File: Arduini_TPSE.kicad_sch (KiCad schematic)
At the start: 29 parts, among them J1 2134441-2, J2 ICSP, P1 Digital, P2 Analog, P3 CONN_01X01, P4 CONN_01X01, P5 CONN_01X01, P6 CONN_01X01, SW1 SW_Push, U1 AMS1117-3.3, U2 FT232RL, U3 ATmega328-P, U4 AMS1117-5.0, Y1 16Mhz

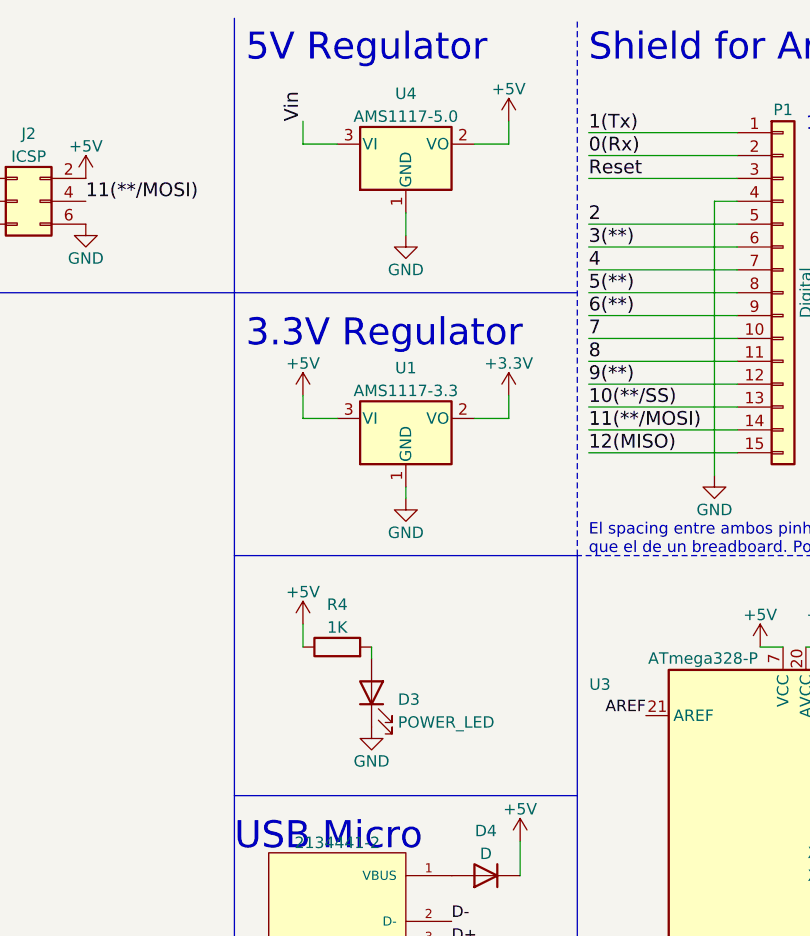
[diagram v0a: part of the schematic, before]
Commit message: Condensadores 3V3, 5V, y recolocacion
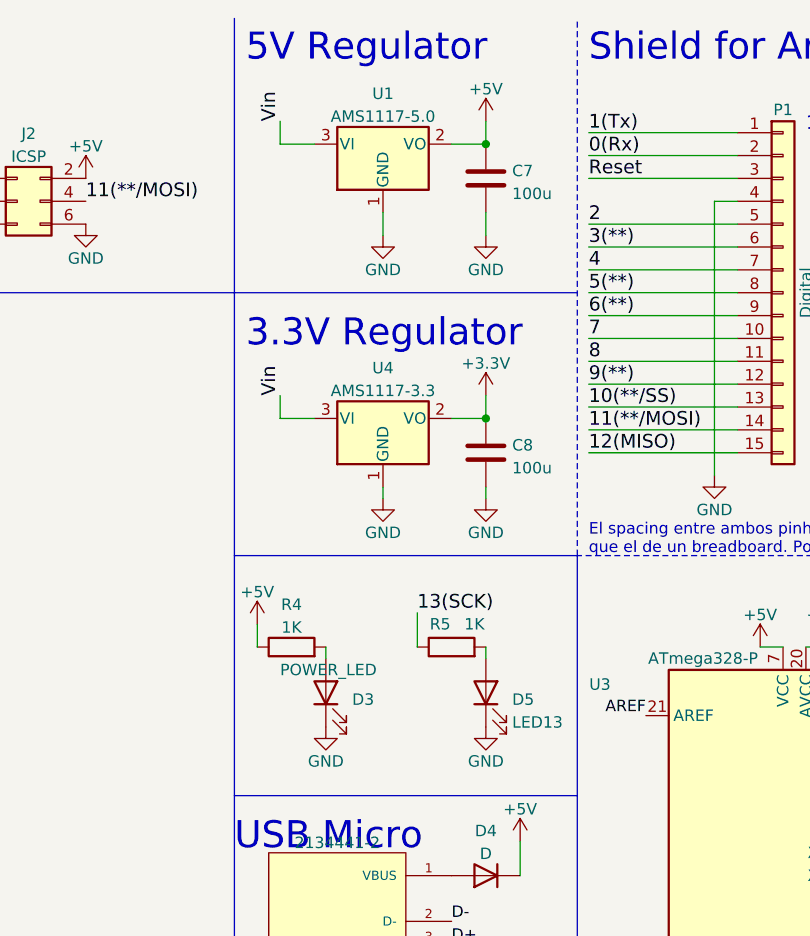
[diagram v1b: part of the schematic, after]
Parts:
- added C7, C8: 100u, Capacitor_SMD:C_1206_3216Metric_Pad1.33x1.80mm_HandSolder, symbol Device:C
- added D5: LED13, LED_THT:LED_D3.0mm, symbol Device:LED
- added R5: 1K, Resistor_SMD:R_1206_3216Metric_Pad1.30x1.75mm_HandSolder, symbol Device:R
- D4: footprint Diode_SMD:D_1210_3225Metric_Pad1.42x2.65mm_HandSolder -> Diode_SMD:D_SMA
- renumbered U4 to U1, U1 to U4
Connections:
- net +3V3: now also C8.1
- net +5V: now also C7.1; no longer U4.3 (VI)
- net 13(SCK): now also R5.1
- net GND: now also C7.2, C8.2, D5.1 (K)
- net Vin: now also U4.3 (VI)
- new net: D5.2 (A), R5.2
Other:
- moved on the sheet: D3, R4, U1, U4

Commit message: Ampliacion
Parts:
- removed D4: D, Diode_SMD:D_SMA, symbol Device:D
- added C10, C8: (no value), Capacitor_SMD:C_1206_3216Metric_Pad1.33x1.80mm_HandSolder, symbol Device:C
- added D1: (no value), symbol Device:D_Schottky
- C7: value 100u -> (none); footprint Capacitor_SMD:C_1206_3216Metric_Pad1.33x1.80mm_HandSolder -> (none)
- C9: renamed from C8; footprint Capacitor_SMD:C_1206_3216Metric_Pad1.33x1.80mm_HandSolder -> (none)
- renumbered D1 to D3, D3 to D4, U4 to U2, U2 to U3, U3 to U4
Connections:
- net +3V3: now also P2.6 (Pin_6), C10.1; no longer P2.5 (Pin_5)
- net +5V: now also U2.3 (VI), C8.1, D1.1 (K)
- net GND: now also P2.5 (Pin_5), C10.2, C8.2; no longer P2.6 (Pin_6)
- net Vin: no longer U2.3 (VI)
- net at J1.1 (VBUS): now also D1.2 (A)
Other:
- moved on the sheet: C7, C9, U1, U2

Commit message: Final
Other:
- title: (none) -> Arduini TPSE
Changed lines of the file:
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@@
   (paper "A4")
   (title_block
-    (date "jeu. 02 avril 2015")
+    (title "Arduini TPSE")
+    (date "2022-03-30")
+    (rev "0.3")
   )
   (junction (at 83.82 160.02) (diameter 0) (color 0 0 0 0)

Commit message: Version presentada
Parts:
- removed C7: (no value), symbol Device:C
- removed C9: 100u, symbol Device:C
- added C7, C9: (no value), symbol Device:C_Polarized
- C10, C8: value (none) -> 100n
- D1: value (none) -> D_Schottky; footprint (none) -> Diode_SMD:D_SMA
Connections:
- net +3V3: now also C9.1
- net +5V: now also C7.1
- net GND: now also C7.2, C9.2
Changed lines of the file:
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@@
   (junction (at 83.82 160.02) (diameter 0) (color 0 0 0 0)
   )
+  (junction (at 201.93 34.29) (diameter 0) (color 0 0 0 0)
+  )
+  (junction (at 203.2 125.73) (diameter 0) (color 0 0 0 0)
+  )
+  (junction (at 260.35 38.1) (diameter 0) (color 0 0 0 0)
+  )
+  (junction (at 201.93 57.15) (diameter 0) (color 0 0 0 0)
+  )
+  (junction (at 45.72 189.23) (diameter 0) (color 0 0 0 0)
+  )
   (junction (at 201.93 64.77) (diameter 0) (color 0 0 0 0)
-  )
-  (junction (at 203.2 125.73) (diameter 0) (color 0 0 0 0)
-  )
-  (junction (at 260.35 38.1) (diameter 0) (color 0 0 0 0)
-  )
-  (junction (at 201.93 34.29) (diameter 0) (color 0 0 0 0)
-  )
-  (junction (at 201.93 57.15) (diameter 0) (color 0 0 0 0)
-  )
-  (junction (at 45.72 189.23) (diameter 0) (color 0 0 0 0)
   )
   (junction (at 201.93 26.67) (diameter 0) (color 0 0 0 0)
@@
       (effects (font (size 1.27 1.27)) (justify left))
     )
-    (property "Value" "" (id 1) (at 209.55 63.5 0)
+    (property "Value" "100n" (id 1) (at 209.55 63.5 0)
       (effects (font (size 1.27 1.27)) (justify left))
     )
@@
     )
     (property "Datasheet" "~" (id 3) (at 208.28 60.96 0)
+      (effects (font (size 1.27 1.27)) hide)
+    )
+    (pin "1")
+    (pin "2")
+  )
+  (symbol (lib_id "Device:C_Polarized") (at 201.93 60.96 0) (unit 1)
+    (in_bom yes) (on_board yes)
+    (property "Reference" "C9" (id 0) (at 196.85 58.42 0)
+      (effects (font (size 1.27 1.27)) (justify left))
+    )
+    (property "Value" "" (id 1) (at 196.85 63.5 0)
+      (effects (font (size 1.27 1.27)) (justify left))
+    )
+    (property "Footprint" "" (id 2) (at 202.8952 64.77 0)
+      (effects (font (size 1.27 1.27)) hide)
+    )
+    (property "Datasheet" "~" (id 3) (at 201.93 60.96 0)
       (effects (font (size 1.27 1.27)) hide)
     )
@@
     )
     (pin "1")
-  )
-  (symbol (lib_id "Device:C") (at 201.93 30.48 0) (unit 1)
-    (in_bom yes) (on_board yes)
-    (property "Reference" "C7" (id 0) (at 196.85 29.21 0)
-      (effects (font (size 1.27 1.27)) (justify left))
-    )
-    (property "Value" "" (id 1) (at 196.85 33.02 0)
-      (effects (font (size 1.27 1.27)) (justify left))
-    )
-    (property "Footprint" "" (id 2) (at 202.8952 34.29 0)
-      (effects (font (size 1.27 1.27)) hide)
-    )
-    (property "Datasheet" "~" (id 3) (at 201.93 30.48 0)
-      (effects (font (size 1.27 1.27)) hide)
-    )
-    (pin "1")
-    (pin "2")
   )
   (symbol (lib_id "Device:R") (at 280.67 82.55 0) (unit 1)
@@
       (effects (font (size 1.27 1.27)) (justify left))
     )
-    (property "Value" "" (id 1) (at 209.55 33.02 0)
+    (property "Value" "100n" (id 1) (at 209.55 33.02 0)
       (effects (font (size 1.27 1.27)) (justify left))
     )
@@
     (pin "1")
   )
+  (symbol (lib_id "Device:C_Polarized") (at 201.93 30.48 0) (unit 1)
+    (in_bom yes) (on_board yes)
+    (property "Reference" "C7" (id 0) (at 196.85 27.94 0)
+      (effects (font (size 1.27 1.27)) (justify left))
+    )
+    (property "Value" "" (id 1) (at 196.85 33.02 0)
+      (effects (font (size 1.27 1.27)) (justify left))
+    )
+    (property "Footprint" "" (id 2) (at 202.8952 34.29 0)
+      (effects (font (size 1.27 1.27)) hide)
+    )
+    (property "Datasheet" "~" (id 3) (at 201.93 30.48 0)
+      (effects (font (size 1.27 1.27)) hide)
+    )
+    (pin "1")
+    (pin "2")
+  )
   (symbol (lib_id "Device:LED") (at 77.47 165.1 90) (unit 1)
     (in_bom yes) (on_board yes)
@@
     (in_bom yes) (on_board yes) (fields_autoplaced)
     (property "Reference" "D1" (id 0) (at 204.7875 102.9802 0))
-    (property "Value" "" (id 1) (at 204.7875 105.5171 0))
-    (property "Footprint" "" (id 2) (at 204.47 107.95 0)
+    (property "Value" "D_Schottky" (id 1) (at 204.7875 105.5171 0))
+    (property "Footprint" "Diode_SMD:D_SMA" (id 2) (at 204.47 107.95 0)
       (effects (font (size 1.27 1.27)) hide)
     )
@@
     (property "Datasheet" "" (id 3) (at 204.47 91.44 0))
     (pin "1")
-  )
-  (symbol (lib_id "Device:C") (at 201.93 60.96 0) (unit 1)
-    (in_bom yes) (on_board yes)
-    (property "Reference" "C9" (id 0) (at 196.85 59.69 0)
-      (effects (font (size 1.27 1.27)) (justify left))
-    )
-    (property "Value" "100u" (id 1) (at 196.85 63.5 0)
-      (effects (font (size 1.27 1.27)) (justify left))
-    )
-    (property "Footprint" "" (id 2) (at 202.8952 64.77 0)
-      (effects (font (size 1.27 1.27)) hide)
-    )
-    (property "Datasheet" "~" (id 3) (at 201.93 60.96 0)
-      (effects (font (size 1.27 1.27)) hide)
-    )
-    (pin "1")
-    (pin "2")
   )
   (symbol (lib_id "power:+5V") (at 83.82 160.02 0) (unit 1)
@@
       (reference "C6") (unit 1) (value "100n") (footprint "Capacitor_SMD:C_1206_3216Metric_Pad1.33x1.80mm_HandSolder")
     )
-    (path "/46c35bc8-3e06-4afa-a332-565364e00f33"
+    (path "/6a31060f-6af7-4ff7-881b-4bd0403498b4"
       (reference "C7") (unit 1) (value "100u") (footprint "Capacitor_Tantalum_SMD:CP_EIA-3528-15_AVX-H_Pad1.50x2.35mm_HandSolder")
     )
@@
       (reference "C8") (unit 1) (value "100n") (footprint "Capacitor_SMD:C_1206_3216Metric_Pad1.33x1.80mm_HandSolder")
     )
-    (path "/e354d1a0-bc02-4502-986b-30666a66a9b1"
+    (path "/313b7a9e-8d80-45a1-a06b-45a9ea7f6767"
       (reference "C9") (unit 1) (value "100u") (footprint "Capacitor_Tantalum_SMD:CP_EIA-3528-15_AVX-H_Pad1.50x2.35mm_HandSolder")
     )
